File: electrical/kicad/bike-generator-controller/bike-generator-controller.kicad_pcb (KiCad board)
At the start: 2 copper layers, 0 parts

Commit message: feat: establish controller PCB V1 design baseline
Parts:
- added C1: 100nF, Capacitor_SMD:C_0805_2012Metric_Pad1.18x1.45mm_HandSolder, F.Cu at (51.0, 93.0)
- added C10: 3.3nF, Capacitor_SMD:C_0805_2012Metric_Pad1.18x1.45mm_HandSolder, F.Cu at (104.0, 90.0)
- added C11: 82pF C0G, Capacitor_SMD:C_0805_2012Metric_Pad1.18x1.45mm_HandSolder, F.Cu at (108.0, 90.0)
- added C12: 100nF X7R, Capacitor_SMD:C_0805_2012Metric_Pad1.18x1.45mm_HandSolder, F.Cu at (102.0, 52.0)
- added C13: 10uF / 100V, Capacitor_SMD:C_1210_3225Metric_Pad1.33x2.70mm_HandSolder, F.Cu at (81.0, 111.0)
- added C2: 1uF, Capacitor_SMD:C_0805_2012Metric_Pad1.18x1.45mm_HandSolder, F.Cu at (55.0, 92.5)
- added C3: 100nF, Capacitor_SMD:C_0805_2012Metric_Pad1.18x1.45mm_HandSolder, F.Cu at (52.0, 100.5)
- added C4: 10uF / 100V, Capacitor_SMD:C_1210_3225Metric_Pad1.33x2.70mm_HandSolder, F.Cu at (79.5, 103.5)
- added C5: 10uF / 100V, Capacitor_SMD:C_1210_3225Metric_Pad1.33x2.70mm_HandSolder, F.Cu at (75.0, 111.0)
- added C6: 10uF / 100V, Capacitor_THT:CP_Radial_D6.3mm_P2.50mm, F.Cu at (111.0, 102.0)
- added C7: 22uF, Capacitor_SMD:C_1210_3225Metric_Pad1.33x2.70mm_HandSolder, F.Cu at (111.0, 94.0)
- added C8: 22uF, Capacitor_SMD:C_1210_3225Metric_Pad1.33x2.70mm_HandSolder, F.Cu at (111.0, 87.0)
- added C9: 2.2nF 50V, Capacitor_SMD:C_0805_2012Metric_Pad1.18x1.45mm_HandSolder, F.Cu at (87.0, 94.0)
- added F1: ABC-V-20-R, BikeGenerator:Fuse_Eaton_ABC-V-20-R_Axial_P38.10mm, F.Cu at (43.0, 127.0)
- added F2: F_AUX / PROVISOIRE, BikeGenerator:Fuse_Littelfuse_0449001MR_6.10x2.69mm, F.Cu at (70.0, 104.0)
- added J1: J_CC_CTRL, Connector_PinHeader_2.54mm:PinHeader_1x03_P2.54mm_Vertical, F.Cu at (116.0, 58.0)
- added J2: J_DISPLAY_I2C, Connector_PinHeader_2.54mm:PinHeader_1x04_P2.54mm_Vertical, F.Cu at (24.0, 36.0)
- added J3: J_DEBUG_UART, Connector_PinHeader_2.54mm:PinHeader_1x04_P2.54mm_Vertical, F.Cu at (24.0, 52.0)
- added J4: PHOENIX 1711725 / RECTIFIER_IN, TerminalBlock_Phoenix:TerminalBlock_Phoenix_MKDS-3-2-5.08_1x02_P5.08mm_Horizontal, F.Cu at (24.0, 113.5)
- added J5: PHOENIX 1711725 / BUCK_IN, TerminalBlock_Phoenix:TerminalBlock_Phoenix_MKDS-3-2-5.08_1x02_P5.08mm_Horizontal, F.Cu at (78.0, 128.0)
- added J6: LiPo 1S / JST-PH 2.0 / PROV., Connector_JST:JST_PH_S2B-PH-K_1x02_P2.00mm_Horizontal, F.Cu at (34.0, 24.5)
- added JP1: ADDR_A0, Jumper:SolderJumper-3_P1.3mm_Bridged12_Pad1.0x1.5mm_NumberLabels, F.Cu at (36.0, 95.0)
- added JP2: ADDR_A1, Jumper:SolderJumper-3_P1.3mm_Bridged12_Pad1.0x1.5mm_NumberLabels, F.Cu at (36.0, 102.0)
- added JP3: GEN 5V / USB INTERLOCK, Connector_PinHeader_2.54mm:PinHeader_1x02_P2.54mm_Vertical, F.Cu at (45.0, 23.0)
- added L1: 47uH, Inductor_SMD:L_Coilcraft_MSS1038-XXX, F.Cu at (99.0, 100.0)
- added R1: 10R, Resistor_SMD:R_0805_2012Metric_Pad1.20x1.40mm_HandSolder, F.Cu at (45.0, 102.0)
- added R10: 200k / 1%, Resistor_SMD:R_0805_2012Metric_Pad1.20x1.40mm_HandSolder, F.Cu at (96.0, 90.0)
- added R11: 316k / 0.1%, Resistor_SMD:R_0805_2012Metric_Pad1.20x1.40mm_HandSolder, F.Cu at (90.0, 108.0)
- added R12: 100k / 0.1%, Resistor_SMD:R_0805_2012Metric_Pad1.20x1.40mm_HandSolder, F.Cu at (96.0, 108.0)
- added R13: 200k / 1%, Resistor_SMD:R_0805_2012Metric_Pad1.20x1.40mm_HandSolder, F.Cu at (100.0, 90.0)
- added R14: 47k, Resistor_SMD:R_0805_2012Metric_Pad1.20x1.40mm_HandSolder, F.Cu at (104.0, 79.0)
- added R2: 10R, Resistor_SMD:R_0805_2012Metric_Pad1.20x1.40mm_HandSolder, F.Cu at (58.0, 102.0)
- added R3: 4.7k, Resistor_SMD:R_0805_2012Metric_Pad1.20x1.40mm_HandSolder, F.Cu at (42.0, 91.0)
- added R4: 4.7k, Resistor_SMD:R_0805_2012Metric_Pad1.20x1.40mm_HandSolder, F.Cu at (42.0, 95.0)
- added R5: 10k, Resistor_SMD:R_0805_2012Metric_Pad1.20x1.40mm_HandSolder, F.Cu at (62.0, 97.0)
- added R6: 10k, Resistor_SMD:R_0805_2012Metric_Pad1.20x1.40mm_HandSolder, F.Cu at (95.0, 58.0)
- added R7: CSS4J-4026K-2L00F 2mR, Resistor_SMD:R_Shunt_Isabellenhuette_BVR4026, F.Cu at (49.0, 112.0)
- added R8: 41.2k / 1%, Resistor_SMD:R_1206_3216Metric_Pad1.30x1.75mm_HandSolder, F.Cu at (78.0, 96.0)
- added R9: 1M / 1%, Resistor_SMD:R_0805_2012Metric_Pad1.20x1.40mm_HandSolder, F.Cu at (78.0, 92.0)
- added S1: 1101M2S3CQE2 / BAT ON-OFF, BikeGenerator:SW_1101M2S3CQE2, F.Cu at (34.0, 39.0)
- added TP1: SHUNT_HI_K, TestPoint:TestPoint_Pad_D1.5mm, F.Cu at (42.0, 106.0)
- added TP10: CC_W, TestPoint:TestPoint_Pad_D1.5mm, F.Cu at (99.0, 66.0)
- added TP11: CC_B, TestPoint:TestPoint_Pad_D1.5mm, F.Cu at (104.0, 66.0)
- added TP12: AUX_IN, TestPoint:TestPoint_Pad_D1.5mm, F.Cu at (70.0, 98.0)
- added TP13: AUX_5V, TestPoint:TestPoint_Pad_D1.5mm, F.Cu at (114.0, 79.0)
- added TP14: AUX_PGOOD, TestPoint:TestPoint_Pad_D1.5mm, F.Cu at (108.0, 74.0)
- added TP15: GND, TestPoint:TestPoint_Pad_D1.5mm, F.Cu at (114.0, 74.0)
- added TP16: GND, TestPoint:TestPoint_Pad_D1.5mm, F.Cu at (51.0, 23.0)
- added TP17: GND, TestPoint:TestPoint_Pad_D1.5mm, F.Cu at (56.0, 23.0)
- added TP2: SHUNT_LO_K, TestPoint:TestPoint_Pad_D1.5mm, F.Cu at (54.5, 106.0)
- added TP3: VBUS_SENSE, TestPoint:TestPoint_Pad_D1.5mm, F.Cu at (63.0, 105.0)
- added TP4: +3V3, TestPoint:TestPoint_Pad_D1.5mm, F.Cu at (36.0, 85.0)
- added TP5: GND, TestPoint:TestPoint_Pad_D1.5mm, F.Cu at (41.0, 85.0)
- added TP6: I2C_SDA, TestPoint:TestPoint_Pad_D1.5mm, F.Cu at (46.0, 85.0)
- added TP7: I2C_SCL, TestPoint:TestPoint_Pad_D1.5mm, F.Cu at (51.0, 85.0)
- added TP8: INA_ALERT, TestPoint:TestPoint_Pad_D1.5mm, F.Cu at (56.0, 85.0)
- added TP9: CC_A, TestPoint:TestPoint_Pad_D1.5mm, F.Cu at (94.0, 66.0)
- added U1: INA228, Package_SO:TSSOP-10_3x3mm_P0.5mm, F.Cu at (52.0, 97.0)
- added U2: DFR0868 Beetle ESP32-C3, BikeGenerator:DFR0868_Beetle_ESP32-C3_V2_Socketed, F.Cu at (104.0, 36.0)
- added U3: MCP4151-104E/SN, Package_SO:SOIC-8_3.9x4.9mm_P1.27mm, F.Cu at (102.0, 58.0)
- added U4: LM5164DDAT, BikeGenerator:SOIC-8-1EP_DDA_EP2.95x4.9mm_6Vias_D0.30mm, F.Cu at (87.0, 100.0)
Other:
- board outline added: 100 x 115 mm

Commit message: feat: route primary power and INA228 Kelvin paths
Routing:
- net GND: track 0.00 -> 68.4 mm
- net Net-(F1-Pad2): track 0.00 -> 41.0 mm
- net /INA228_SENSE/VBUS_SENSE: track 0.00 -> 32.0 mm
- net /INA228_SENSE/SHUNT_HI_K: track 0.00 -> 22.3 mm
- net /INA228_SENSE/SHUNT_LO_K: track 0.00 -> 21.1 mm
- net Net-(J4-Pin_1): track 0.00 -> 13.5 mm
- net /INA228_SENSE/INA_IN_PLUS: track 0.00 -> 13.2 mm
- net /INA228_SENSE/INA_IN_MINUS: track 0.00 -> 12.7 mm
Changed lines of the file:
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@@
 		(layer "Edge.Cuts")
+	)
+	(segment
+		(start 88 128)
+		(end 83.08 128)
+		(width 5)
+		(layer "B.Cu")
+		(net "GND")
+	)
+	(segment
+		(start 70 117)
+		(end 88 128)
+		(width 5)
+		(layer "B.Cu")
+		(net "GND")
+	)
+	(segment
+		(start 32.58 117)
+		(end 70 117)
+		(width 5)
+		(layer "B.Cu")
+		(net "GND")
+	)
+	(segment
+		(start 29.08 113.5)
+		(end 32.58 117)
+		(width 5)
+		(layer "B.Cu")
+		(net "GND")
+	)
+	(segment
+		(start 24 113.5)
+		(end 23.95 127)
+		(width 5)
+		(layer "F.Cu")
+		(net "Net-(J4-Pin_1)")
+	)
+	(segment
+		(start 50.1 106)
+		(end 54.5 106)
+		(width 0.25)
+		(layer "F.Cu")
+		(net "/INA228_SENSE/SHUNT_LO_K")
+	)
+	(segment
+		(start 54.5 106)
+		(end 58 103)
+		(width 0.25)
+		(layer "F.Cu")
+		(net "/INA228_SENSE/SHUNT_LO_K")
+	)
+	(segment
+		(start 53.025 115.2)
+		(end 50.1 115.2)
+		(width 0.25)
+		(layer "F.Cu")
+		(net "/INA228_SENSE/SHUNT_LO_K")
+	)
+	(segment
+		(start 50.1 115.2)
+		(end 50.1 106)
+		(width 0.25)
+		(layer "F.Cu")
+		(net "/INA228_SENSE/SHUNT_LO_K")
+	)
+	(segment
+		(start 76.85 128)
+		(end 78 128)
+		(width 5)
+		(layer "F.Cu")
+		(net "/INA228_SENSE/VBUS_SENSE")
+	)
+	(segment
+		(start 53.025 111.15)
+		(end 60 111.15)
+		(width 5)
+		(layer "F.Cu")
+		(net "/INA228_SENSE/VBUS_SENSE")
+	)
+	(segment
+		(start 60 111.15)
+		(end 76.85 128)
+		(width 5)
+		(layer "F.Cu")
+		(net "/INA228_SENSE/VBUS_SENSE")
+	)
+	(segment
+		(start 47.9 115.2)
+		(end 47.9 106)
+		(width 0.25)
+		(layer "F.Cu")
+		(net "/INA228_SENSE/SHUNT_HI_K")
+	)
+	(segment
+		(start 44.975 115.2)
+		(end 47.9 115.2)
+		(width 0.25)
+		(layer "F.Cu")
+		(net "/INA228_SENSE/SHUNT_HI_K")
+	)
+	(segment
+		(start 47.9 106)
+		(end 42 106)
+		(width 0.25)
+		(layer "F.Cu")
+		(net "/INA228_SENSE/SHUNT_HI_K")
+	)
+	(segment
+		(start 42 106)
+		(end 45 103)
+		(width 0.25)
+		(layer "F.Cu")
+		(net "/INA228_SENSE/SHUNT_HI_K")
+	)
+	(segment
+		(start 48 127)
+		(end 38 117)
+		(width 5)
+		(layer "F.Cu")
+		(net "Net-(F1-Pad2)")
+	)
+	(segment
+		(start 38 117)
+		(end 38 111.15)
+		(width 5)
+		(layer "F.Cu")
+		(net "Net-(F1-Pad2)")
+	)
+	(segment
+		(start 38 111.15)
+		(end 44.975 111.15)
+		(width 5)
+		(layer "F.Cu")
+		(net "Net-(F1-Pad2)")
+	)
+	(segment
+		(start 62.05 127)
+		(end 48 127)
+		(width 5)
+		(layer "F.Cu")
+		(net "Net-(F1-Pad2)")
+	)
+	(segment
+		(start 53.5 100.0375)
+		(end 55.5 100.0375)
+		(width 0.25)
+		(layer "F.Cu")
+		(net "/INA228_SENSE/INA_IN_MINUS")
+	)
+	(segment
+		(start 53.0375 100.5)
+		(end 53.5 100.0375)
+		(width 0.25)
+		(layer "F.Cu")
+		(net "/INA228_SENSE/INA_IN_MINUS")
+	)
+	(segment
+		(start 53.5375 101)
+		(end 53.0375 100.5)
+		(width 0.25)
+		(layer "F.Cu")
+		(net "/INA228_SENSE/INA_IN_MINUS")
+	)
+	(segment
+		(start 55.5 100.0375)
+		(end 55.5 96.5)
+		(width 0.25)
+		(layer "F.Cu")
+		(net "/INA228_SENSE/INA_IN_MINUS")
+	)
+	(segment
+		(start 58 101)
+		(end 53.5375 101)
+		(width 0.25)
+		(layer "F.Cu")
+		(net "/INA228_SENSE/INA_IN_MINUS")
+	)
+	(segment
+		(start 55.5 96.5)
+		(end 54.150001 96.5)
+		(width 0.25)
+		(layer "F.Cu")
+		(net "/INA228_SENSE/INA_IN_MINUS")
+	)
+	(segment
+		(start 45 101)
+		(end 50.4625 101)
+		(width 0.25)
+		(layer "F.Cu")
+		(net "/INA228_SENSE/INA_IN_PLUS")
+	)
+	(segment
+		(start 50.9625 100.5)
+		(end 52 99.4625)
+		(width 0.25)
+		(layer "F.Cu")
+		(net "/INA228_SENSE/INA_IN_PLUS")
+	)
+	(segment
+		(start 50.4625 101)
+		(end 50.9625 100.5)
+		(width 0.25)
+		(layer "F.Cu")
+		(net "/INA228_SENSE/INA_IN_PLUS")
+	)
+	(segment
+		(start 52 96)
+		(end 54.150001 96)
+		(width 0.25)
+		(layer "F.Cu")
+		(net "/INA228_SENSE/INA_IN_PLUS")
+	)
+	(segment
+		(start 52 99.4625)
+		(end 52 96)
+		(width 0.25)
+		(layer "F.Cu")
+		(net "/INA228_SENSE/INA_IN_PLUS")
 	)
 	(embedded_fonts no)

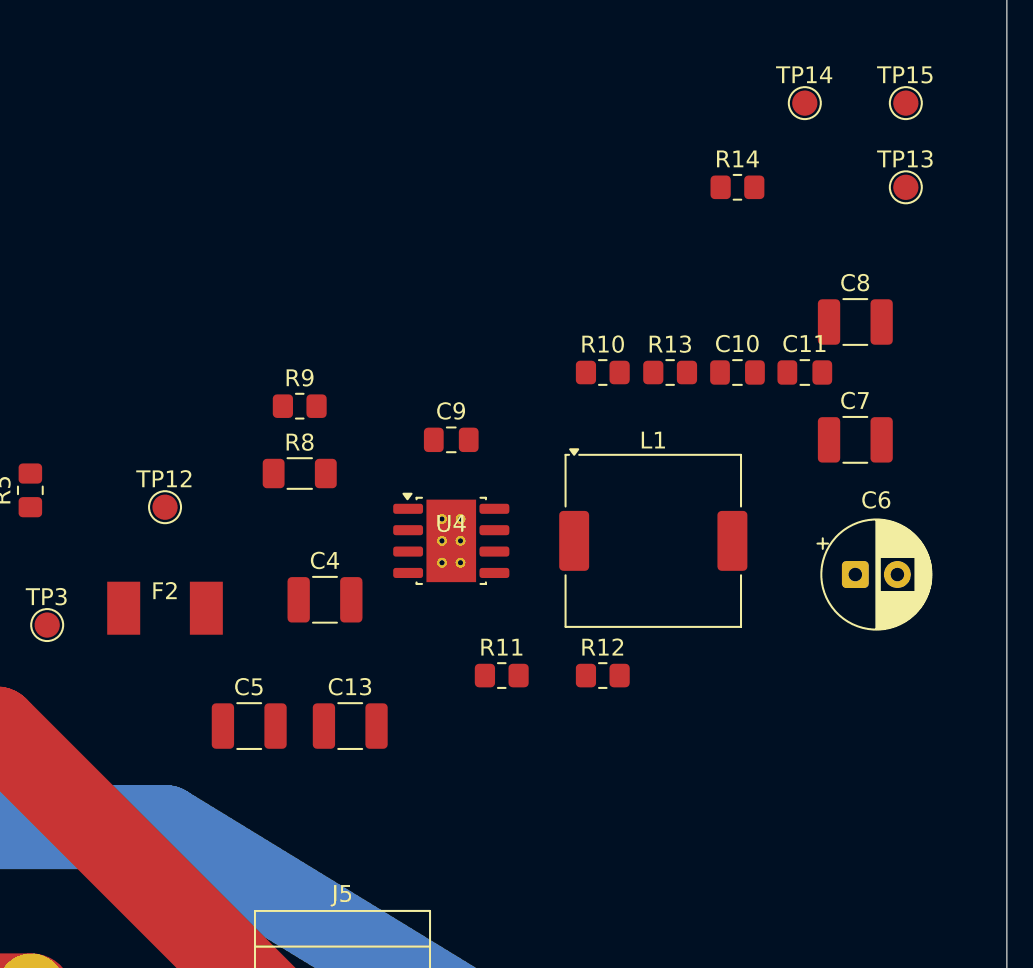
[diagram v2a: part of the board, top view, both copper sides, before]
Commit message: feat: route LM5164 auxiliary supply
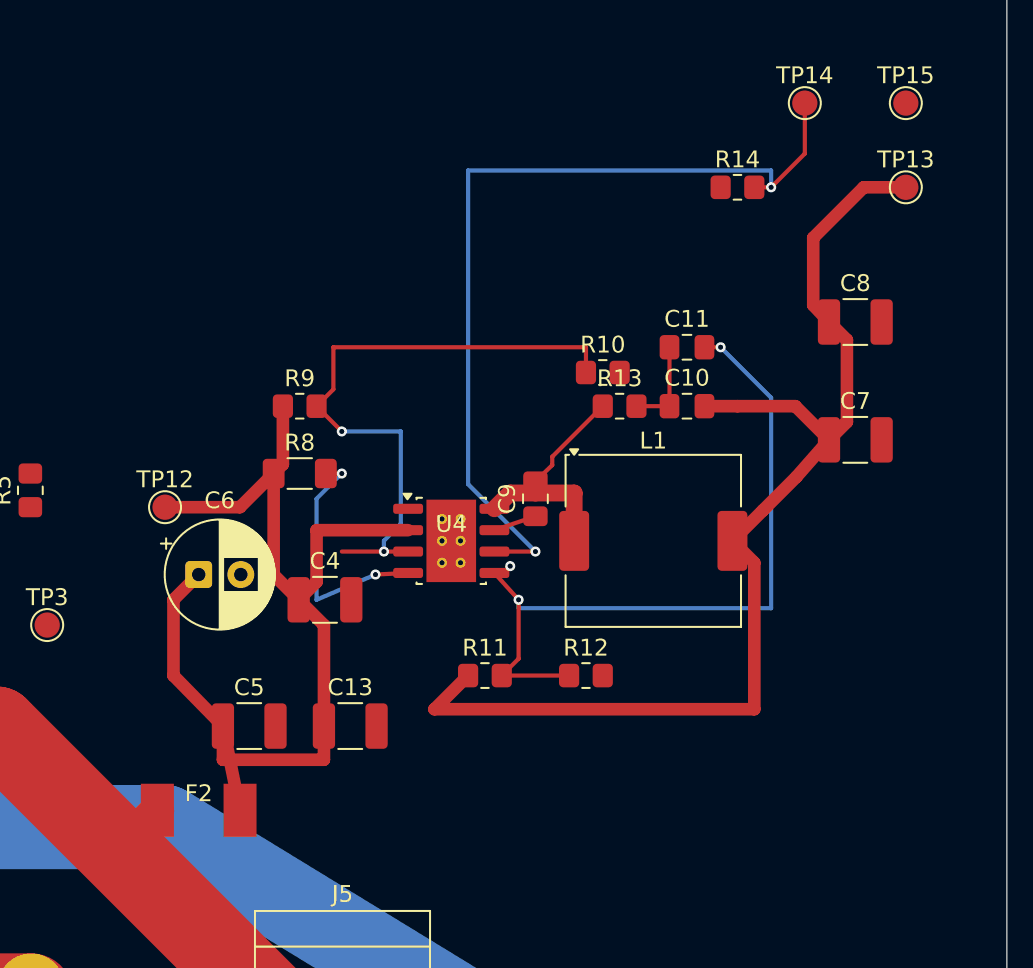
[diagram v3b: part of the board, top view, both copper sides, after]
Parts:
- moved C6 39.0 mm to (72.0, 102.0)
- moved F2 12.2 mm to (72.0, 116.0)
- moved C11 7.16 mm to (101.0, 88.5)
- moved C9 6.10 mm to (92.0, 97.5), turned to 90 degrees
- moved C10 3.61 mm to (101.0, 92.0)
- moved R13 3.61 mm to (97.0, 92.0)
- moved R11 1.00 mm to (89.0, 108.0)
- moved R12 1.00 mm to (95.0, 108.0)
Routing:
- net /AUX_SUPPLY/AUX_5V: track 0.00 -> 68.9 mm
- net /AUX_SUPPLY/AUX_IN_PROTECTED: track 0.00 -> 63.7 mm
- net /AUX_SUPPLY/AUX_PGOOD: track 0.00 -> 52.6 mm, vias 0 -> 2
- net /AUX_SUPPLY/FB: track 0.00 -> 44.3 mm, vias 0 -> 3
- net /AUX_SUPPLY/UVLO: track 0.00 -> 37.5 mm, vias 0 -> 2
- net /AUX_SUPPLY/RON_SET: track 0.00 -> 14.8 mm, vias 0 -> 2
- net /AUX_SUPPLY/SW: track 0.00 -> 14.8 mm
- net /AUX_SUPPLY/RIPPLE: track 0.00 -> 5.46 mm
- net /INA228_SENSE/VBUS_SENSE: track 32.0 -> 35.3 mm
- net /AUX_SUPPLY/BST: track 0.00 -> 2.57 mm

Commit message: wip: checkpoint controller routing before review
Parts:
- removed the C2 at (55.0, 92.5)
- removed the J3 at (24.0, 52.0)
- removed TP10: CC_W, TestPoint:TestPoint_Pad_D1.5mm
- removed TP11: CC_B, TestPoint:TestPoint_Pad_D1.5mm
- removed the TP14 at (108.0, 74.0)
- removed TP15, TP16, TP17: GND, TestPoint:TestPoint_Pad_D1.5mm
- removed TP3: VBUS_SENSE, TestPoint:TestPoint_Pad_D1.5mm
- removed the TP4 at (36.0, 85.0)
- removed the TP5 at (41.0, 85.0)
- removed TP9: CC_A, TestPoint:TestPoint_Pad_D1.5mm
- added C3: 1uF, Capacitor_SMD:C_0805_2012Metric_Pad1.18x1.45mm_HandSolder, F.Cu at (90.0, 114.0)
- added D1: SMCJ70A, Diode_SMD:D_SMC, F.Cu at (84.6, 120.5)
- added D2: DBI25-16A / 3PH BRIDGE, BikeGenerator:Diode_Bridge_Diotec_DBI-A_5Pin_P7.50mm, F.Cu at (73.8, 104.9)
- added J5: J_EXT_GPIO, Connector_JST:JST_PH_S4B-PH-K_1x04_P2.00mm_Horizontal, F.Cu at (76.4, 22.6)
- added J8: 3PH_GEN_IN (1=U 2=V 3=W), TerminalBlock_Phoenix:TerminalBlock_Phoenix_MKDS-3-3-5.08_1x03_P5.08mm_Horizontal, F.Cu at (61.7, 111.4)
- added J9: J_CV_CTRL, Connector_PinHeader_2.54mm:PinHeader_1x03_P2.54mm_Vertical, F.Cu at (68.8, 66.9)
- added R10: 1k, Resistor_SMD:R_0805_2012Metric_Pad1.20x1.40mm_HandSolder, F.Cu at (82.6, 31.3)
- added R19: 10k, Resistor_SMD:R_0805_2012Metric_Pad1.20x1.40mm_HandSolder, F.Cu at (81.5, 56.7)
- added R7: 10k, Resistor_SMD:R_0805_2012Metric_Pad1.20x1.40mm_HandSolder, F.Cu at (91.1, 28.4)
- added R8: 10k, Resistor_SMD:R_0805_2012Metric_Pad1.20x1.40mm_HandSolder, F.Cu at (80.5, 35.4)
- added R9: 1k, Resistor_SMD:R_0805_2012Metric_Pad1.20x1.40mm_HandSolder, F.Cu at (80.4, 31.3)
- C5: renamed from C13; value 10uF / 100V -> 10uF/100V
- C6: value 10uF / 100V -> 10uF/100V
- C7: renamed from C4; value 10uF / 100V -> 10uF/100V
- C8: renamed from C5; value 10uF / 100V -> 10uF/100V
- C9: value 2.2nF 50V -> 2.2nF/50V
- F1: value ABC-V-20-R -> 0456020.ER / 20A; footprint BikeGenerator:Fuse_Eaton_ABC-V-20-R_Axial_P38.10mm -> BikeGenerator:Fuse_Littelfuse_456_10.08x3.05mm_P9.35mm
- J1: renamed from J4; value PHOENIX 1711725 / RECTIFIER_IN -> DC_GEN_IN / DNP (DC VARIANT)
- R12: renamed from R8; value 41.2k / 1% -> 41.2k/1%
- R13: renamed from R9; value 1M / 1% -> 1M/1%
- R14: renamed from R10; value 200k / 1% -> 200k/1%
- R16: renamed from R13; value 200k / 1% -> 200k/1%
- R17: renamed from R11; value 316k / 0.1% -> 316k/0.1%
- R18: renamed from R12; value 100k / 0.1% -> 100k/0.1%
- TP12: value AUX_IN -> ~
- U3: value MCP4151-104E/SN -> MCP42100-I/SL; footprint Package_SO:SOIC-8_3.9x4.9mm_P1.27mm -> Package_SO:SOIC-14_3.9x8.7mm_P1.27mm
- moved J3 65.0 mm to (78.2, 71.8), turned to -90 degrees
- moved JP2 60.6 mm to (96.5, 97.5), turned to 0 degrees
- moved JP1 60.5 mm to (96.5, 101.5), turned to 0 degrees
- moved R2 52.1 mm to (95.5, 115.0)
- moved TP1 49.8 mm to (90.5, 117.5)
- moved R6 47.9 mm to (88.0, 104.5)
- moved R4 47.2 mm to (89.0, 99.5)
- moved TP4 47.2 mm to (90.0, 102.0), turned to -90 degrees
- moved R1 46.9 mm to (94.5, 123.5), turned to 180 degrees
- moved TP2 45.2 mm to (98.5, 116.5)
- moved C13 45.1 mm to (96.1, 51.4)
- moved JP3 45.0 mm to (88.3, 35.0)
- moved TP5 44.1 mm to (88.9, 107.6), turned to -90 degrees
- moved C2 43.9 mm to (94.5, 111.5), turned to 180 degrees
- moved C1 43.2 mm to (90.0, 111.5), turned to 180 degrees
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- renumbered C11 to C10, C10 to C11, C8 to C12, C7 to C13, C3 to C2, C12 to C4, J5 to J2, J2 to J3, J1 to J7, JP2 to JP1, JP1 to JP2, R7 to R1, R6 to R11, R14 to R15, R1 to R2, R2 to R3, R3 to R6, TP13 to TP14, TP6 to TP4, TP7 to TP5, TP8 to TP6
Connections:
- net /INA228_SENSE/INA_A0 renamed Net-(JP2-C)
- net /INA228_SENSE/INA_A1 renamed Net-(JP1-C)
- net Net-(J4-Pin_1) renamed /POWER_PATH/RECTIFIED_RAW
- C1 pad 1: +3V3 -> GND
- C1 pad 2: GND -> +3V3
- C4 pad 1: +3V3 -> GND
- C4 pad 2: GND -> +3V3
- F1 pad 2: Net-(F1-Pad2) -> Net-(D1-K)
- J2 pad 1: /INA228_SENSE/VBUS_SENSE -> GND
- J2 pad 2: GND -> /INA228_SENSE/VBUS_SENSE
- R1 pad 1: Net-(F1-Pad2) -> /INA228_SENSE/VBUS_SENSE
- R1 pad 2: /INA228_SENSE/SHUNT_HI_K -> /INA228_SENSE/SHUNT_LO_K
- R1 pad 3: /INA228_SENSE/SHUNT_LO_K -> /INA228_SENSE/SHUNT_HI_K
- R1 pad 4: /INA228_SENSE/VBUS_SENSE -> Net-(D1-K)
- R4 pad 2: /I2C_SCL -> /I2C_SDA
- R6 pad 2: /I2C_SDA -> /I2C_SCL
- U2 pad 12: /UART_RX -> /POT_SHDN
- U2 pad 14: Net-(U2-GPIO8) -> /CONNECTORS/GPIO8_ACTION
- U2 pad 15: Net-(U2-GPIO9_BOOT) -> unconnected-(U2-GPIO9_BOOT-Pad15)
- U2 pad 5: unconnected-(U2-GPIO4-Pad5) -> /CONNECTORS/GPIO4_HALL
- U3 pad 5: /CC_CONTROL/CC_A -> /CC_CONTROL/CV_B
- U3 pad 6: /CC_CONTROL/CC_W -> /CC_CONTROL/CV_W
- U3 pad 7: /CC_CONTROL/CC_B -> /CC_CONTROL/CV_A
- U3 pad 8: +3V3 -> /CC_CONTROL/CC_A
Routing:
- net +3V3: track 0.00 -> 280.8 mm, vias 0 -> 9
- net /I2C_SCL: track 0.00 -> 148.7 mm, vias 0 -> 4
- net /I2C_SDA: track 0.00 -> 147.1 mm, vias 0 -> 4
- net /INA_ALERT: track 0.00 -> 118.8 mm, vias 0 -> 6
- net /CC_CONTROL/POT_MOSI: track 0.00 -> 93.1 mm, vias 0 -> 2
- net /CC_CONTROL/POT_CS: track 0.00 -> 86.1 mm, vias 0 -> 2
- net /CC_CONTROL/POT_SCK: track 0.00 -> 84.5 mm, vias 0 -> 2
- net /CONNECTORS/GPIO4_HALL: track 0.00 -> 67.8 mm, vias 0 -> 2
- net /AUX_SUPPLY/AUX_PGOOD: track 52.6 -> 2.41 mm, vias 2 -> 0
- net /POT_SHDN: track 0.00 -> 44.5 mm
- net Net-(F1-Pad2): track 41.0 -> 0.00 mm
- net /AUX_SUPPLY/FB: track 44.3 -> 9.40 mm, vias 3 -> 0
- net GND: track 68.4 -> 34.9 mm, vias 0 -> 17
- net /AUX_SUPPLY/UVLO: track 37.5 -> 9.32 mm, vias 2 -> 0
- net /MCU/BAT_CTRL: track 0.00 -> 27.2 mm, vias 0 -> 2
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- added copper zone on B.Cu, net GND
